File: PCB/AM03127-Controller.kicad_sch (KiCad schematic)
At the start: 13 parts, among them U1 XIAO-ESP32-C3-DIP, U2 MAX3232, U3 AMS1117 5.0

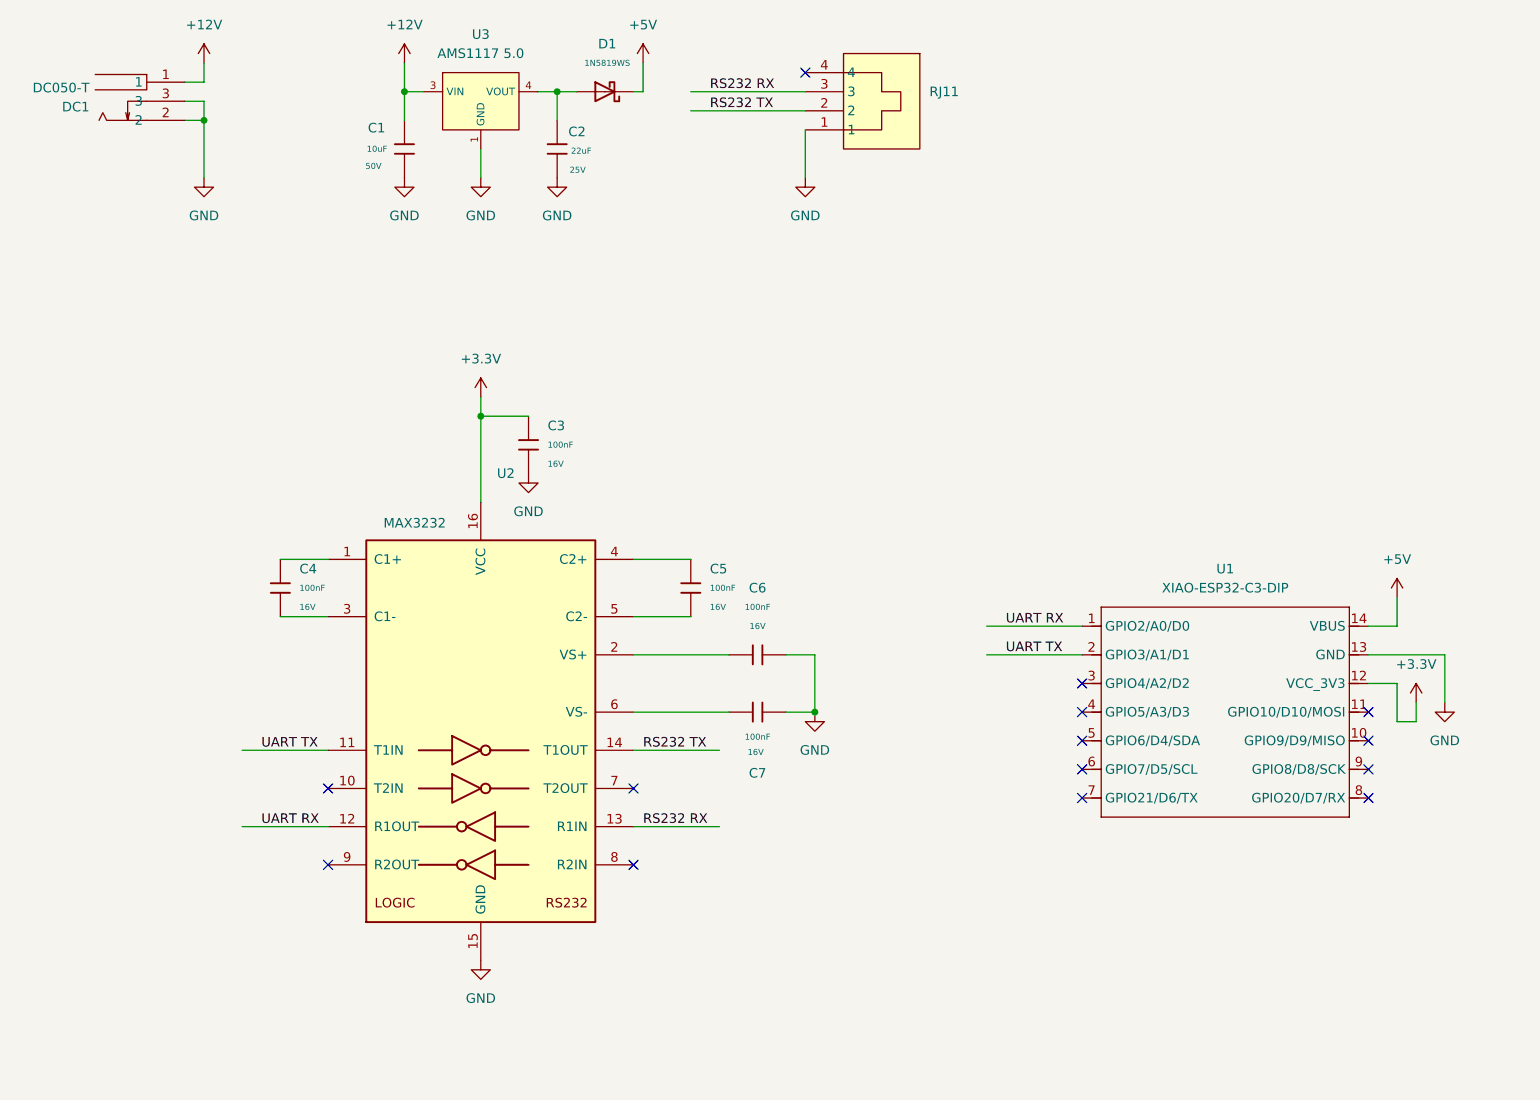
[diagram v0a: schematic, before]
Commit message: Refactor LDO to Buckconverter
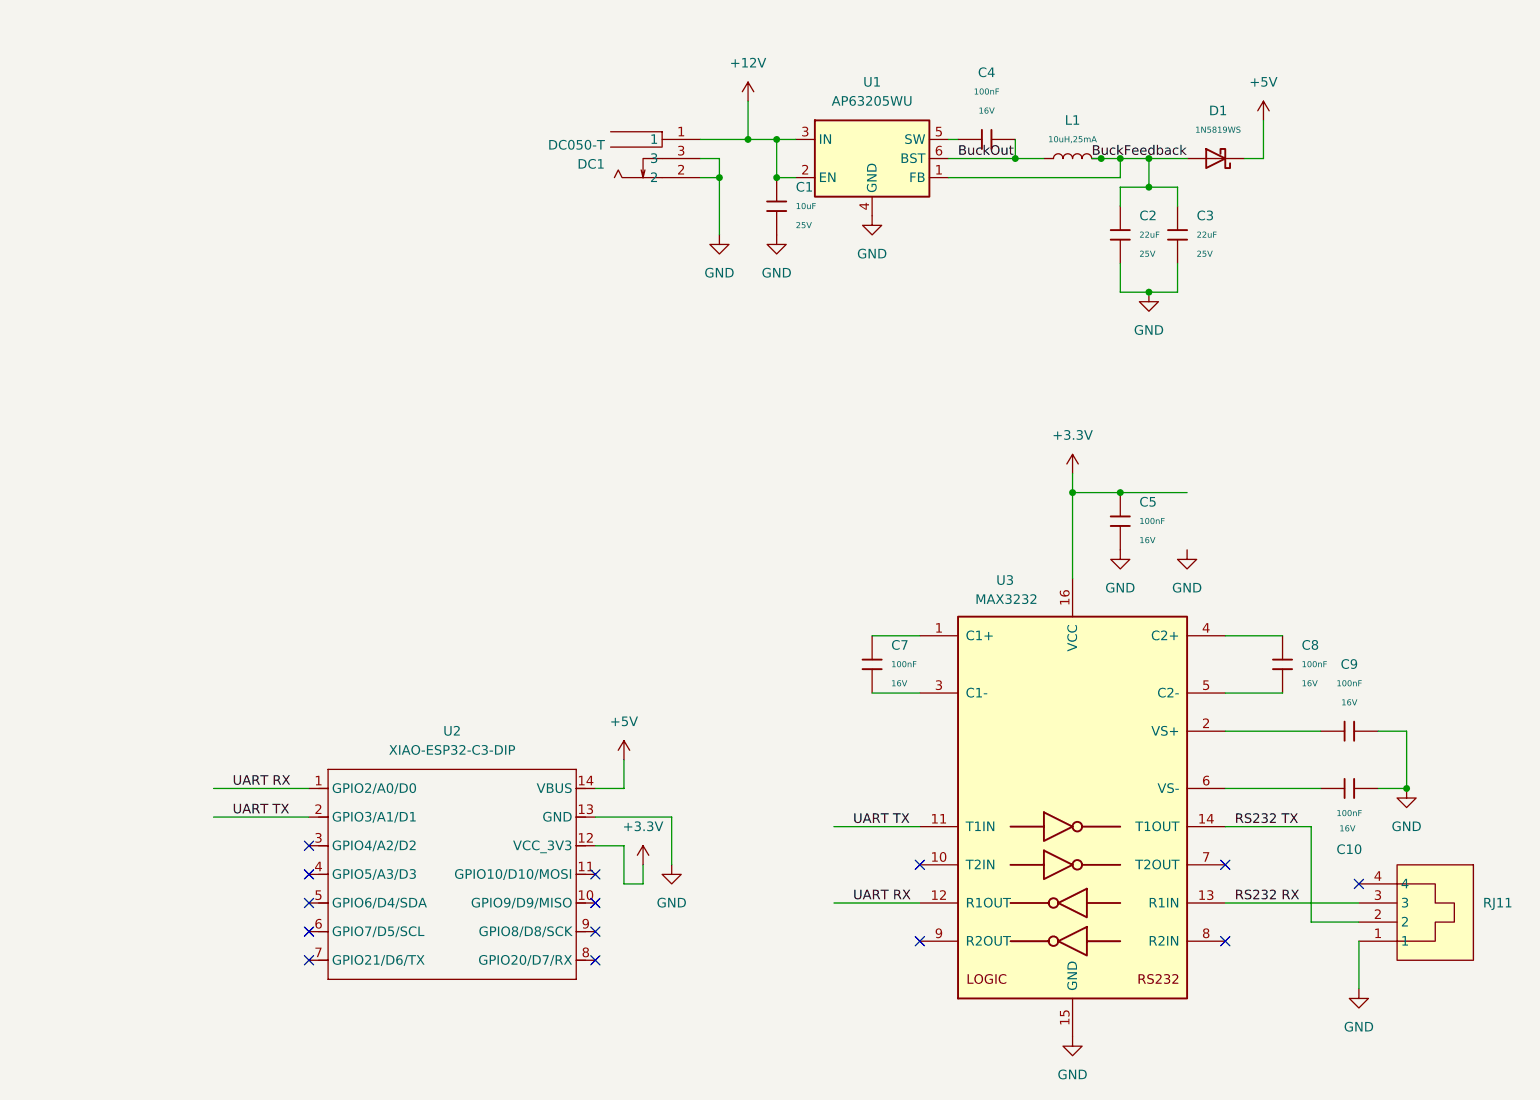
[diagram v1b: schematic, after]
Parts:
- removed C1: 10uF, PCM_JLCPCB:C_1206, symbol PCM_JLCPCB-Capacitors:1206,10uF
- removed C2: 22uF, PCM_JLCPCB:C_1206, symbol PCM_JLCPCB-Capacitors:1206,22uF,(2)
- removed U3: AMS1117 5.0, PCM_JLCPCB:SOT-223_L6.5-W3.5-P2.30-LS7.0-BR, symbol PCM_JLCPCB-Power:LDO, 5V, 1A
- added C1: 10uF, PCM_JLCPCB:C_0805, symbol PCM_JLCPCB-Capacitors:0805,10uF
- added C2, C3: 22uF, PCM_JLCPCB:C_0805, symbol PCM_JLCPCB-Capacitors:0805,22uF
- added C4: 100nF, PCM_JLCPCB:C_0402, symbol PCM_JLCPCB-Capacitors:0402,100nF
- added L1: 10uH,25mA, PCM_JLCPCB:L_1206, symbol PCM_JLCPCB-Inductors:10uH,25mA
- added U1: AP63205WU, Package_TO_SOT_SMD:TSOT-23-6, symbol Regulator_Switching:AP63205WU
- renumbered C7 to C10, C3 to C5, C4 to C7, C5 to C8, C6 to C9, U1 to U2, U2 to U3
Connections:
- net +12V: now also C1.1, U1.2 (EN), U1.3 (IN)
- net GND: now also C1.2, C2.2, C3.2, U1.4 (GND)
- net BuckFeedback: now reaches D1.2
- net BuckFeedback: now also C2.1, C3.1, L1.2, U1.1 (FB)
- new net: C4.1, U1.5 (SW)
- new net BuckOut: C4.2, L1.1, U1.6 (BST)
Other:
- moved on the sheet: C10, C5, C7, C8, C9, D1, DC1, RJ11, U2, U3

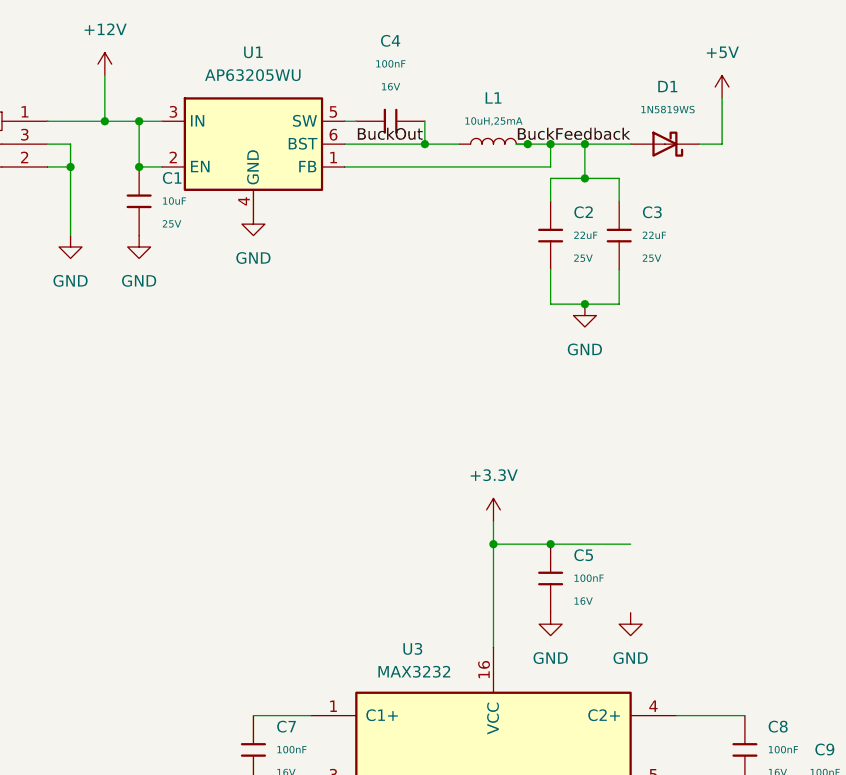
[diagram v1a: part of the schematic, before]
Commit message: Refactor PCB using buttom GND Plate
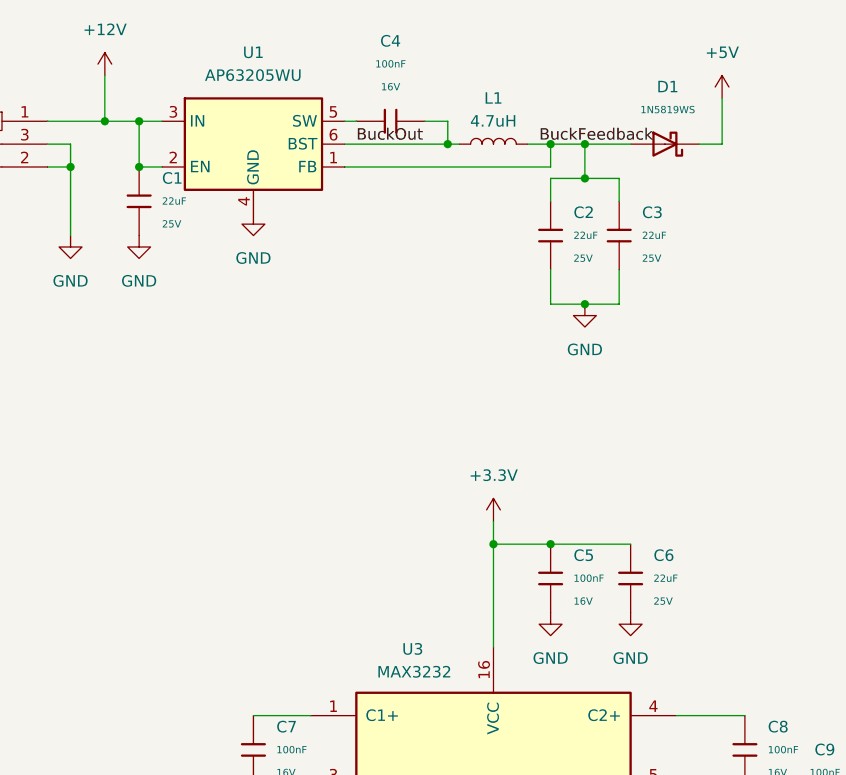
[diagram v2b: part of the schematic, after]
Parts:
- removed C1: 10uF, PCM_JLCPCB:C_0805, symbol PCM_JLCPCB-Capacitors:0805,10uF
- removed C2, C3: 22uF, PCM_JLCPCB:C_0805, symbol PCM_JLCPCB-Capacitors:0805,22uF
- removed L1: 10uH,25mA, PCM_JLCPCB:L_1206, symbol PCM_JLCPCB-Inductors:10uH,25mA
- added C1, C2, C3, C6: 22uF, PCM_JLCPCB:C_1206, symbol PCM_JLCPCB-Capacitors:1206,22uF,(2)
- added L1: 4.7uH, Inductor_SMD:L_1008_2520Metric, symbol Device:L
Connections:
- net +12V: now also C1.1
- net +3.3V: now also C6.1
- net BuckFeedback: now also C2.1, C3.1, L1.2
- net BuckOut: now also L1.1
- net GND: now also C1.2, C2.2, C3.2, C6.2

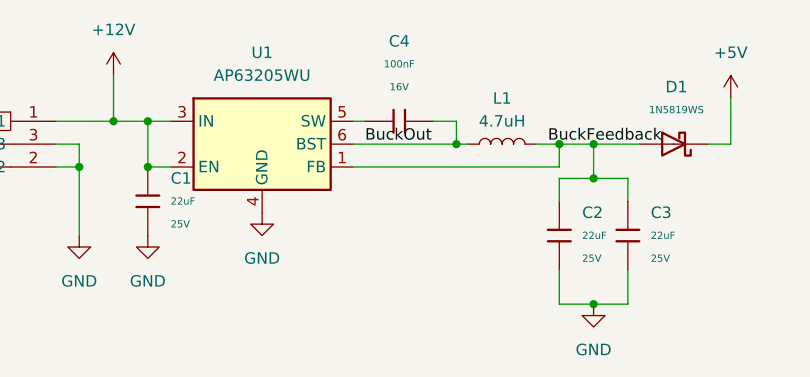
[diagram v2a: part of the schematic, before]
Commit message: Fix swaped pin for voltage regulator in PCB
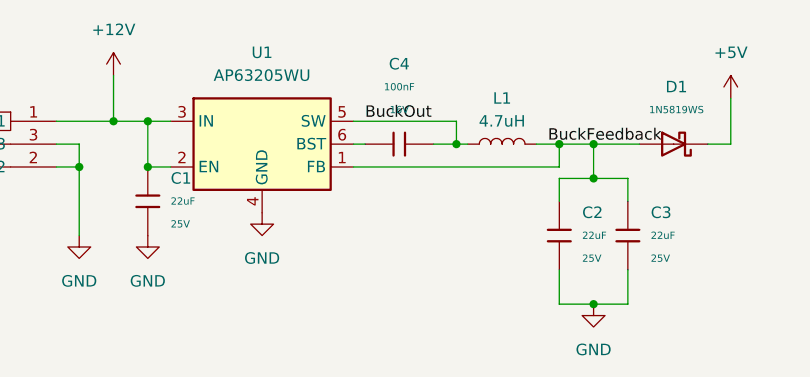
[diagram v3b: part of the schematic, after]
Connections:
- net BuckOut: now also U1.5 (SW); no longer U1.6 (BST)
- net at C4.1: now also U1.6 (BST); no longer U1.5 (SW)
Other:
- moved on the sheet: C4
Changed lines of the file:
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@@
 	)
 	(junction
+		(at 151.13 43.18)
+		(diameter 0)
+		(color 0 0 0 0)
+	)
+	(junction
 		(at 166.37 46.99)
 		(diameter 0)
@@
 	)
 	(junction
-		(at 151.13 43.18)
-		(diameter 0)
-		(color 0 0 0 0)
-	)
-	(junction
 		(at 116.84 45.72)
 		(diameter 0)
@@
 	(wire
 		(pts
-			(xy 139.7 40.64) (xy 140.97 40.64)
+			(xy 148.59 43.18) (xy 151.13 43.18)
 		)
 		(stroke
@@
 	(wire
 		(pts
-			(xy 113.03 35.56) (xy 113.03 40.64)
+			(xy 139.7 40.64) (xy 151.13 40.64)
 		)
 		(stroke
@@
 	(wire
 		(pts
-			(xy 181.61 38.1) (xy 181.61 43.18)
+			(xy 113.03 35.56) (xy 113.03 40.64)
 		)
 		(stroke
@@
 	(wire
 		(pts
-			(xy 109.22 43.18) (xy 109.22 45.72)
+			(xy 181.61 38.1) (xy 181.61 43.18)
 		)
 		(stroke
@@
 	(wire
 		(pts
-			(xy 92.71 127) (xy 96.52 127)
+			(xy 109.22 43.18) (xy 109.22 45.72)
 		)
 		(stroke
@@
 	(wire
 		(pts
-			(xy 151.13 40.64) (xy 148.59 40.64)
+			(xy 92.71 127) (xy 96.52 127)
 		)
 		(stroke
@@
 	(wire
 		(pts
-			(xy 139.7 43.18) (xy 151.13 43.18)
+			(xy 151.13 40.64) (xy 151.13 43.18)
 		)
 		(stroke
@@
 	(wire
 		(pts
-			(xy 151.13 40.64) (xy 151.13 43.18)
-		)
-		(stroke
-			(width 0)
-			(type default)
-		)
-	)
-	(wire
-		(pts
 			(xy 162.56 46.99) (xy 162.56 49.53)
 		)
@@
 	(wire
 		(pts
+			(xy 139.7 43.18) (xy 140.97 43.18)
+		)
+		(stroke
+			(width 0)
+			(type default)
+		)
+	)
+	(wire
+		(pts
 			(xy 116.84 45.72) (xy 119.38 45.72)
 		)
@@
 	)
 	(label "BuckOut"
-		(at 140.97 43.18 0)
+		(at 140.97 40.64 0)
 		(effects
 			(font
@@
 	(symbol
 		(lib_id "PCM_JLCPCB-Capacitors:0402,100nF")
-		(at 144.78 40.64 90)
+		(at 144.78 43.18 90)
 		(unit 1)
 		(exclude_from_sim no)
@@
 		(fields_autoplaced yes)
 		(property "Reference" "C4"
-			(at 144.78 31.75 90)
+			(at 144.78 34.29 90)
 			(effects
 				(font
@@
 		)
 		(property "Value" "100nF"
-			(at 144.78 34.29 90)
+			(at 144.78 36.83 90)
 			(effects
 				(font
@@
 		)
 		(property "Footprint" "PCM_JLCPCB:C_0402"
-			(at 144.78 42.418 90)
+			(at 144.78 44.958 90)
 			(effects
 				(font
@@
 		)
 		(property "Datasheet" "https://www.lcsc.com/datasheet/lcsc_datasheet_2304140030_Samsung-Electro-Mechanics-CL05B104KO5NNNC_C1525.pdf"
-			(at 144.78 40.64 0)
+			(at 144.78 43.18 0)
 			(effects
 				(font
@@
 		)
 		(property "Description" "16V 100nF X7R ±10% 0402 Multilayer Ceramic Capacitors MLCC - SMD/SMT ROHS"
-			(at 144.78 40.64 0)
+			(at 144.78 43.18 0)
 			(effects
 				(font
@@
 		)
 		(property "LCSC" "C1525"
-			(at 144.78 40.64 0)
+			(at 144.78 43.18 0)
 			(effects
 				(font
@@
 		)
 		(property "Stock" "20208285"
-			(at 144.78 40.64 0)
+			(at 144.78 43.18 0)
 			(effects
 				(font
@@
 		)
 		(property "Price" "0.004USD"
-			(at 144.78 40.64 0)
+			(at 144.78 43.18 0)
 			(effects
 				(font
@@
 		)
 		(property "Process" "SMT"
-			(at 144.78 40.64 0)
+			(at 144.78 43.18 0)
 			(effects
 				(font
@@
 		)
 		(property "Minimum Qty" "20"
-			(at 144.78 40.64 0)
+			(at 144.78 43.18 0)
 			(effects
 				(font
@@
 		)
 		(property "Attrition Qty" "10"
-			(at 144.78 40.64 0)
+			(at 144.78 43.18 0)
 			(effects
 				(font
@@
 		)
 		(property "Class" "Basic Component"
-			(at 144.78 40.64 0)
+			(at 144.78 43.18 0)
 			(effects
 				(font
@@
 		)
 		(property "Category" "Capacitors,Multilayer Ceramic Capacitors MLCC - SMD/SMT"
-			(at 144.78 40.64 0)
+			(at 144.78 43.18 0)
 			(effects
 				(font
@@
 		)
 		(property "Manufacturer" "Samsung Electro-Mechanics"
-			(at 144.78 40.64 0)
+			(at 144.78 43.18 0)
 			(effects
 				(font
@@
 		)
 		(property "Part" "CL05B104KO5NNNC"
-			(at 144.78 40.64 0)
+			(at 144.78 43.18 0)
 			(effects
 				(font
@@
 		)
 		(property "Voltage Rated" "16V"
-			(at 144.78 36.83 90)
+			(at 144.78 39.37 90)
 			(effects
 				(font
@@
 		)
 		(property "Tolerance" "±10%"
-			(at 144.78 40.64 0)
+			(at 144.78 43.18 0)
 			(effects
 				(font
@@
 		)
 		(property "Capacitance" "100nF"
-			(at 144.78 40.64 0)
+			(at 144.78 43.18 0)
 			(effects
 				(font
@@
 		)
 		(property "Temperature Coefficient" "X7R"
-			(at 144.78 40.64 0)
+			(at 144.78 43.18 0)
 			(effects
 				(font
